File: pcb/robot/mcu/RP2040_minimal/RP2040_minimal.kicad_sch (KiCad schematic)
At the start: 44 parts, among them J2 Conn_01x05, U14 TPS3808G01DBVR, U15 TPS3808G01DBVR, U2 W25Q128JVS, U3 RP2040, Y1 ECS-120-8-36-CKM-TR3

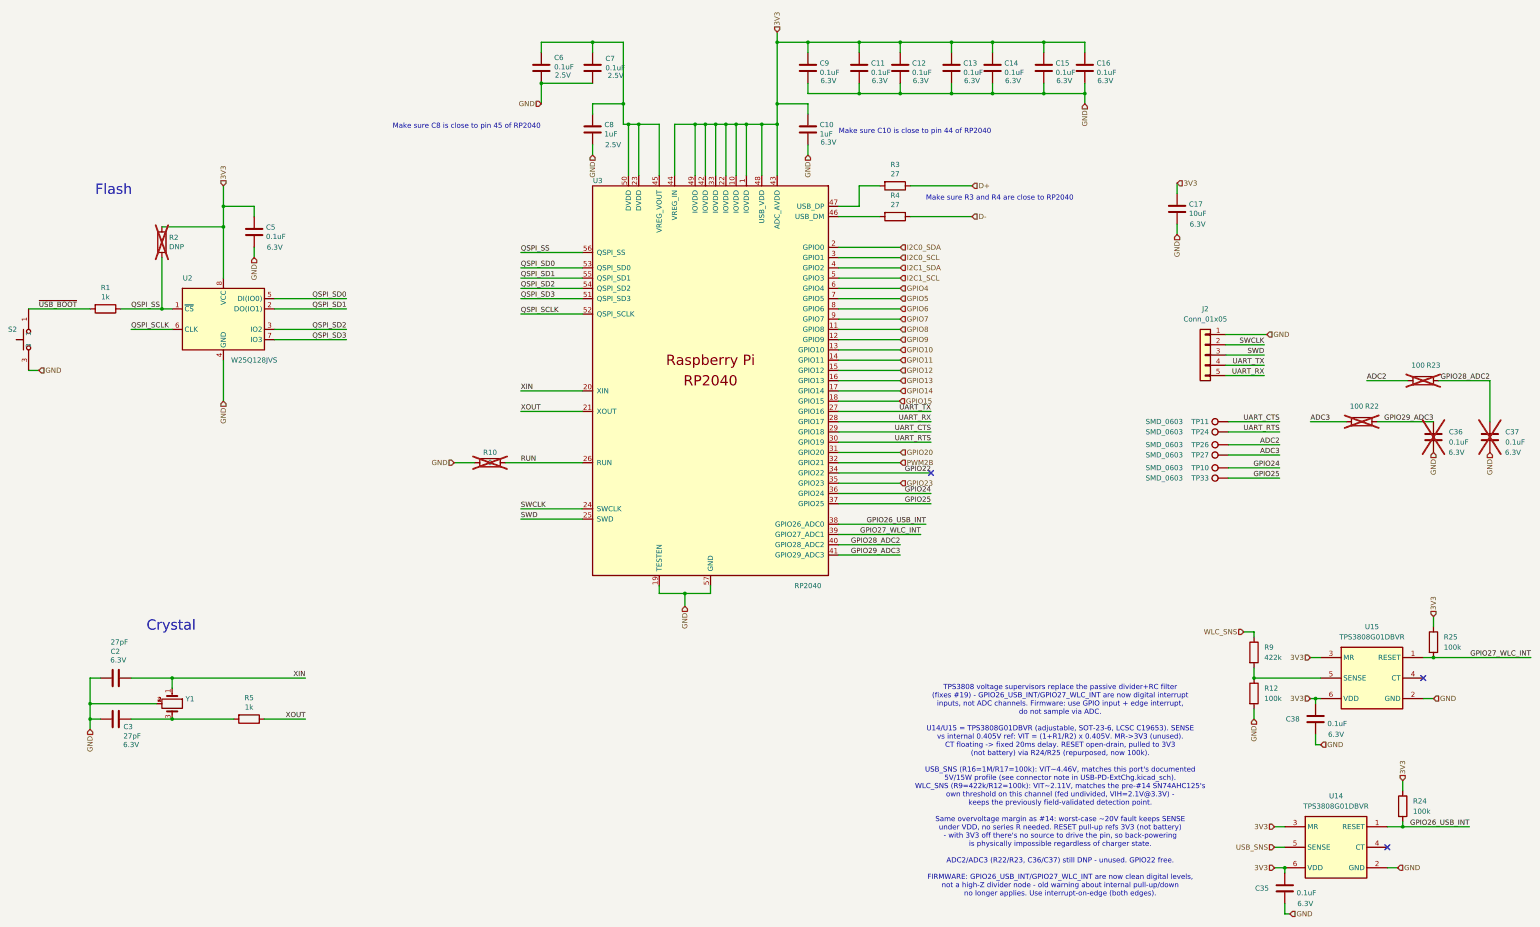
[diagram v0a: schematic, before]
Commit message: Re-unify USB-PD module into main board (single-PCB architecture) (#17)
Merges the USB-PD module circuitry back into the main robot board as
a single PCB, reversing the earlier main-board/USB-PD-daughter-board
split. Full re-route and re-placement of the combined design:

- Consolidated low-profile parts toward the board center, using the
  space freed up by relocated capacitors, for better overall use of
  the available area.
- Kept all 0-ohm test/isolation jumpers in accessible locations for
  bench testing.
- Added/corrected footprints for several parts that had broken or
  incorrect footprints (DDC6_TEX variants, SOT-23-6, SOT-23-3,
  R0402).

Carries forward every closed correction issue and update made since
the original split: #3 (CC jumpers), #6 (IC1.ON pull-down), #14/#15
(ADC divider, motor connector pinout), #16, #18 (I2C isolation
jumpers), #19 (charger-sense GPIO interrupt), plus the BOM/pricing
updates, LED changes, and MAX77642 replacement.

Verified via kicad-cli ERC/DRC + netlist diff against the pre-merge
board: 0 unconnected items (unchanged), no new DRC error-level
violations besides one pre-existing excluded item, and the #6
(IC1.ON pull-down) and #19 (charger-sense GPIO interrupt) circuits
confirmed intact at the net-topology level despite the full-board
re-annotation changing most reference designators. Most of the raw
diff size is a KiCad 9 footprint-format upgrade (pre-2023 format
rewritten to current) rather than design changes - spot-checked
against unrelated footprints (e.g. mounting holes), which show
identical geometry under the new syntax.
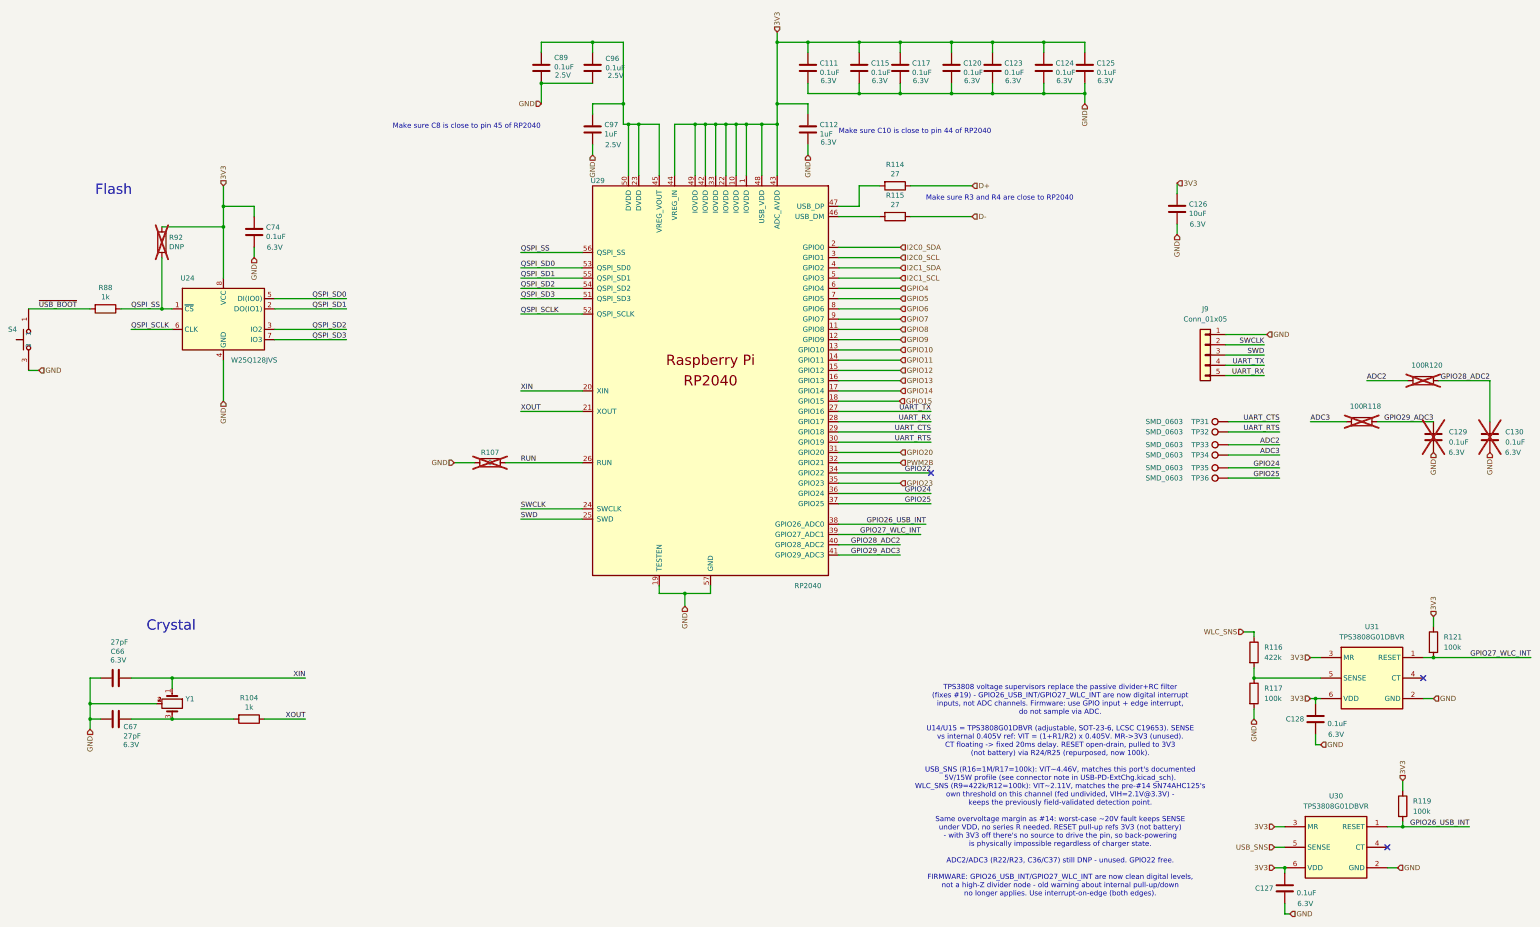
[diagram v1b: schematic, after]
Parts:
- J9: renamed from J2; symbol Connector_Generic:Conn_01x05 -> robot:Conn_01x05
- R107: renamed from R10; symbol Device:R -> robot:R
- U30: renamed from U14; symbol easyeda2kicad:TPS3808G01DBVR -> robot:TPS3808G01DBVR
- U31: renamed from U15; symbol easyeda2kicad:TPS3808G01DBVR -> robot:TPS3808G01DBVR
- renumbered C9 to C111, C10 to C112, C11 to C115, C12 to C117, C13 to C120, C14 to C123, C15 to C124, C16 to C125, C17 to C126, C35 to C127, C38 to C128, C36 to C129, C37 to C130, C2 to C66, C3 to C67, C5 to C74, C6 to C89, C7 to C96, C8 to C97, R5 to R104, R3 to R114, R4 to R115, R9 to R116, R12 to R117, R22 to R118, R24 to R119, R23 to R120, R25 to R121, R1 to R88, R2 to R92, S2 to S4, TP11 to TP31, TP24 to TP32, TP26 to TP33, TP27 to TP34, TP10 to TP35, TP33 to TP36, U2 to U24, U3 to U29
